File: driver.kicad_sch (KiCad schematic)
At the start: 83 parts, among them J2 Conn_02x07_Counter_Clockwise, Q1 RJK0355DSP, Q2 RJK0355DSP, Q3 SiRC18DP, Q4 SiRC18DP, Q5 SiRC18DP, Q6 SiRC18DP, U2 LM3743, U3 MAX1978, U4 INA333xxDGK

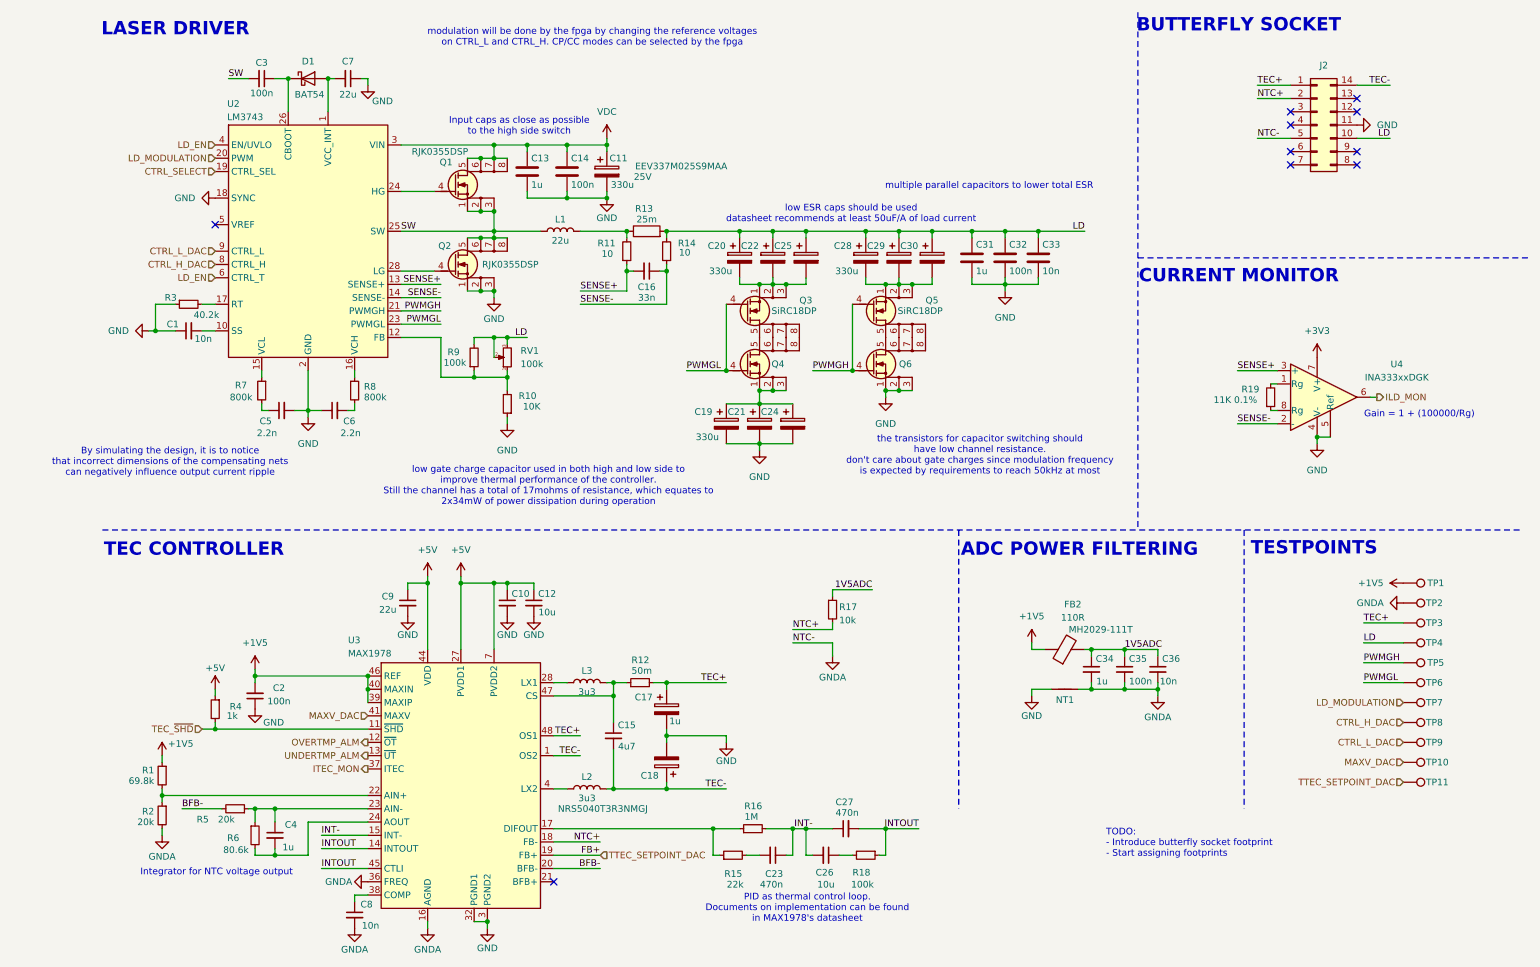
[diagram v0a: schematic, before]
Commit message: update PCB: fixed buck layout, concept layout for LD driver with LT3743
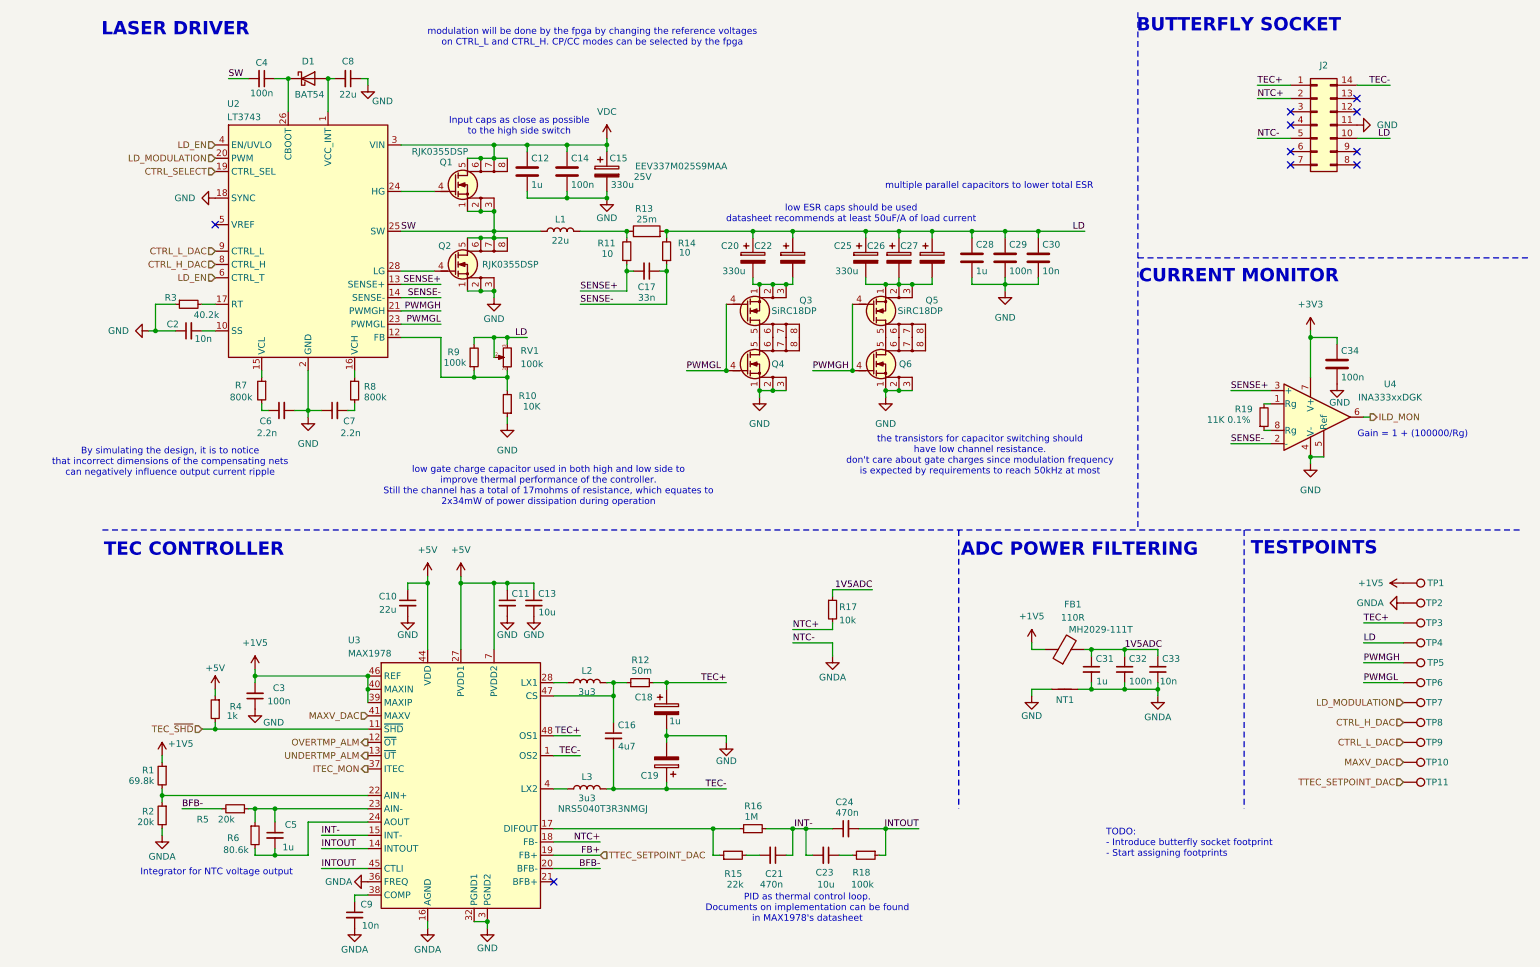
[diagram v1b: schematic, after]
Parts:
- removed C19, C21, C24, C25: 330u, Capacitor_SMD:CP_Elec_8x10.5, symbol Device:C_Polarized
- added C34: 100n, Capacitor_SMD:C_0805_2012Metric, symbol Device:C
- J2: footprint (none) -> footprints:Butterfly_14pins_SMD
- U2: value LM3743 -> LT3743
- renumbered C9 to C10, C10 to C11, C13 to C12, C12 to C13, C11 to C15, C15 to C16, C16 to C17, C17 to C18, C18 to C19, C1 to C2, C23 to C21, C26 to C23, C27 to C24, C28 to C25, C29 to C26, C30 to C27, C31 to C28, C32 to C29, C2 to C3, C33 to C30, C34 to C31, C35 to C32, C36 to C33, C3 to C4, C4 to C5, C5 to C6, C6 to C7, C7 to C8, C8 to C9, FB2 to FB1, L3 to L2, L2 to L3
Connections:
- net +3V3: now also C34.1
- net GND: now also Q4.1 (S), Q4.2 (S), Q4.3 (S), C34.2
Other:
- moved on the sheet: C20, C22, R19, U4

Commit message: Changed overall subsystem positions, TEC controller implemented, LD controller IC position to be reconsidered in order to have enough clearance after header connector is fully routed
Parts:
- added NT3: NetTie_2, NetTie:NetTie-2_SMD_Pad0.5mm, symbol Device:NetTie_2
- TP1, TP11: footprint TestPoint:TestPoint_Pad_D1.5mm -> TestPoint:TestPoint_Pad_D1.0mm
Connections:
- net AGND: now also NT3.2
- net GND: now also U3.49 (EP), NT3.1
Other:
- note removed: "TODO: - Introduce butterfly socket footprint - Start assigning footprints"

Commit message: PCB routing completed, started uniforming components for smaller BOM
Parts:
- C10, C11, C13, C21, C23, C24: footprint Capacitor_SMD:C_0805_2012Metric -> Capacitor_SMD:C_0603_1608Metric; Voltage Rating (none) -> 6V3
- C16, C8: Voltage Rating (none) -> 25V
- C17: Voltage Rating (none) -> 6V3
- C2, C30, C33, C9: Voltage Rating 25V -> 6V3
- C3, C31, C32, C34, C5: footprint Capacitor_SMD:C_0805_2012Metric -> Capacitor_SMD:C_0603_1608Metric; Voltage Rating 25V -> 6V3
- TP10: footprint TestPoint:TestPoint_Pad_D1.5mm -> TestPoint:TestPoint_Pad_D1.0mm

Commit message: small corrections to PCB, fixed some capacitors' voltage ratings and footprints to make BOM more uniform
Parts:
- C16: Voltage Rating 25V -> 16V
- C8: footprint Capacitor_SMD:C_0805_2012Metric -> Capacitor_SMD:C_0603_1608Metric; Voltage Rating 25V -> 6V3
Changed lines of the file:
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@@
 			)
 		)
-		(property "Footprint" "Capacitor_SMD:C_0805_2012Metric"
+		(property "Footprint" "Capacitor_SMD:C_0603_1608Metric"
 			(at 59.69 25.4 0)
 			(effects
@@
 			)
 		)
-		(property "Voltage Rating" "25V"
+		(property "Voltage Rating" "6V3"
 			(at 59.69 25.4 0)
 			(effects
@@
 			)
 		)
-		(property "Voltage Rating" "25V"
+		(property "Voltage Rating" "16V"
 			(at 110.49 151.13 0)
 			(effects

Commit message: feat: made possible to swap butterfly pins for compatibility
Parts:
- added J4: SELECTOR, Connector_PinHeader_2.54mm:PinHeader_2x09_P2.54mm_Vertical, symbol Connector_Generic:Conn_02x09_Odd_Even
- added J5: Conn_02x07_Counter_Clockwise, Connector_PinHeader_2.54mm:PinHeader_1x04_P2.54mm_Vertical, symbol Connector_Generic:Conn_01x04
- J2: value Conn_02x07_Counter_Clockwise -> BUTTERFLY
- TP2: footprint TestPoint:TestPoint_Pad_2.5x2.5mm -> TestPoint:TestPoint_Pad_1.5x1.5mm
- TP8, TP9: footprint TestPoint:TestPoint_Pad_D1.5mm -> TestPoint:TestPoint_Pad_D1.0mm
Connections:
- net AGND: now also J4.11 (Pin_11); no longer J2.5 (Pin_5)
- net GND: now also J4.3 (Pin_3), J4.5 (Pin_5); no longer J2.11 (Pin_11)
- net LD: now also J4.1 (Pin_1); no longer J2.10 (Pin_10)
- net NTC+: now also J4.13 (Pin_13); no longer J2.2 (Pin_2)
- net TEC+: now also J4.9 (Pin_9); no longer J2.1 (Pin_1)
- net TEC-: now also J4.7 (Pin_7); no longer J2.14 (Pin_14)
- net Pin_12: now reaches J2.12 (Pin_12)
- net Pin_12: now also J4.14 (Pin_14)
- net Pin_13: now reaches J2.13 (Pin_13)
- net Pin_13: now also J5.1 (Pin_1)
- net Pin_3: now reaches J2.3 (Pin_3)
- net Pin_3: now also J4.4 (Pin_4)
- net Pin_4: now reaches J2.4 (Pin_4)
- net Pin_4: now also J4.2 (Pin_2)
- net Pin_6: now reaches J2.6 (Pin_6)
- net Pin_6: now also J4.16 (Pin_16)
- net Pin_7: now reaches J2.7 (Pin_7)
- net Pin_7: now also J4.18 (Pin_18)
- net Pin_8: now reaches J2.8 (Pin_8)
- net Pin_8: now also J5.4 (Pin_4)
- net Pin_9: now reaches J2.9 (Pin_9)
- net Pin_9: now also J5.3 (Pin_3)
- new net Pin_1: J2.1 (Pin_1), J4.10 (Pin_10)
- new net Pin_10: J2.10 (Pin_10), J5.2 (Pin_2)
- new net Pin_11: J2.11 (Pin_11), J4.12 (Pin_12)
- new net Pin_14: J2.14 (Pin_14), J4.8 (Pin_8)
- new net Pin_2: J2.2 (Pin_2), J4.17 (Pin_17)
- new net Pin_5: J2.5 (Pin_5), J4.6 (Pin_6)
- no-connect marks 10 -> 3
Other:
- moved on the sheet: J2

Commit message: feat: added method to swap butterfly socket pins to adapt to multiple SOA SNs. Fixed routing imperfections and addes informative silkscreen
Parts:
- R12: value 50m -> 200m
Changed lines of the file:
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@@
 			)
 		)
-		(property "Value" "50m"
-			(at 117.856 138.684 90)
+		(property "Value" "200m"
+			(at 118.364 138.684 90)
 			(effects
 				(font

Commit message: fix: small corrections to the pcb, added PNs and store link to mouser for each component
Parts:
- C10, C8: PN (none) -> GRM188R60J226MEA0D; Store Link (none) -> https://www.mouser.it/ProductDetail/Murata-Electronics/GRM1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
- C11, C13, C23: PN (none) -> GRM188R60J106KE7J; Store Link (none) -> https://www.mouser.it/ProductDetail/Murata-Electronics/GRM1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
- C12, C28: PN (none) -> 885012207078; Store Link (none) -> https://www.mouser.it/ProductDetail/Wurth-Elektronik/885012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
- C14, C29, C4: PN (none) -> CL21F104ZBANNNC; Store Link (none) -> https://www.mouser.it/ProductDetail/Samsung-Electro-Mechani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
- C15, C20, C22, C25, C26, C27: Store Link (none) -> https://www.mouser.it/ProductDetail/KEMET/EEV337M025S9MAA?q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
- C16: PN (none) -> C1608X5R1E475K080AC; Store Link (none) -> https://www.mouser.it/ProductDetail/TDK/C1608X5R1E475K080AC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
- C17: PN (none) -> CGA3E2X7R1H333MA; Store Link (none) -> https://www.mouser.it/ProductDetail/KEMET/C0603C333M5RACTU?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
- C18, C19: PN EEV337M025S9MAA -> EDH105M050A9BAA; Store Link (none) -> https://www.mouser.it/ProductDetail/KEMET/EDH105M050A9BAA?q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
- C2, C30, C33, C9: PN (none) -> C0603C103M5RAC3121; Store Link (none) -> https://www.mouser.it/ProductDetail/KEMET/C0603C103M5RAC312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
- C21, C24: PN (none) -> 885012106020; Store Link (none) -> https://www.mouser.it/ProductDetail/Wurth-Elektronik/885012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
- C3, C32, C34: PN (none) -> CL10B104KB8NNND; Store Link (none) -> https://www.mouser.it/ProductDetail/Samsung-Electro-Mechani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
- C31, C5: PN (none) -> MCASE168SB7105KTNA01; Store Link (none) -> https://www.mouser.it/ProductDetail/TAIYO-YUDEN/MCASE168SB7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
- C6, C7: PN (none) -> C0603C222J3RACTU; Store Link (none) -> https://www.mouser.it/ProductDetail/KEMET/C0603C222J3RACTU?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
- D1: PN (none) -> BAT54; Store Link (none) -> https://www.mouser.it/ProductDetail/Diotec-Semiconductor/BA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; Voltage Rating (none) -> 30V
- FB1: Store Link (none) -> https://www.mouser.it/ProductDetail/Bourns/MH2029-111T?qs=H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
- J2, J4, TP1, TP10, TP11, TP2, TP3, TP4, TP5, TP6, TP7, TP8, TP9: now left out of the parts list
- J5: value Conn_02x07_Counter_Clockwise -> SELECTOR_2; now left out of the parts list
- L1: Store Link (none) -> https://www.mouser.it/ProductDetail/TAIYO-YUDEN/NRS8040T220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
- L2, L3: Store Link (none) -> https://www.mouser.it/ProductDetail/TAIYO-YUDEN/NRS5040T3R3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
- Q1, Q2: PN (none) -> RJK0355DSP; Store Link (none) -> https://www.mouser.it/ProductDetail/Renesas-Electronics/RJK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
- Q3, Q4, Q5, Q6: PN (none) -> SiRC18DP; Store Link (none) -> https://www.mouser.it/ProductDetail/Vishay-Semiconductors/S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
- R1: PN (none) -> ERJ-PB3B6982V; Store Link (none) -> https://www.mouser.it/ProductDetail/Panasonic/ERJ-PB3B6982V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
- R10: value 10K -> 1k; PN (none) -> RC0603FR-7W1KL; Store Link (none) -> https://www.mouser.it/ProductDetail/YAGEO/RC0603FR-7W1KL?qs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
- R11, R14: PN (none) -> CRCW060310R0FKEAC; Store Link (none) -> https://www.mouser.it/ProductDetail/Vishay-Dale/CRCW060310R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
- R12: PN (none) -> 560050350011; Store Link (none) -> https://www.mouser.it/ProductDetail/Wurth-Elektronik/560050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
- R13: value 25m -> 50m; PN (none) -> 560050332001; Store Link (none) -> https://www.mouser.it/ProductDetail/Wurth-Elektronik/560050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
- R15: PN (none) -> RC0603FR-7W22KL; Store Link (none) -> https://www.mouser.it/ProductDetail/YAGEO/RC0603FR-7W22KL?q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
- R16: PN (none) -> CRCW06031M00JNEA; Store Link (none) -> https://www.mouser.it/ProductDetail/Vishay-Dale/CRCW06031M0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
- R17: PN (none) -> CRCW060310K0FKEC; Store Link (none) -> https://www.mouser.it/ProductDetail/Vishay-Dale/CRCW060310K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
- R18: PN (none) -> RC0603FR-10100KL; Store Link (none) -> https://www.mouser.it/ProductDetail/YAGEO/RC0603FR-10100KL?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
- R19: PN (none) -> ERJ-PB3B1102V; Store Link (none) -> https://www.mouser.it/ProductDetail/Panasonic/ERJ-PB3B1102V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
- R2, R5: PN (none) -> ERJ-PB3B2002V; Store Link (none) -> https://www.mouser.it/ProductDetail/Panasonic/ERJ-PB3B2002V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
- R3: PN (none) -> ERJ-PB3B4022V; Store Link (none) -> https://www.mouser.it/ProductDetail/Panasonic/ERJ-PB3B4022V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
- R4: PN (none) -> RC0603FR-7W1KL; Store Link (none) -> https://www.mouser.it/ProductDetail/YAGEO/RC0603FR-7W1KL?qs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
- R6: PN (none) -> ERJ-3RBD8062V; Store Link (none) -> https://www.mouser.it/ProductDetail/Panasonic/ERJ-3RBD8062V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
- R7, R8: value 800k -> 806k; PN (none) -> CRCW0603806KFKEA; Store Link (none) -> https://www.mouser.it/ProductDetail/Vishay-Dale/CRCW0603806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
- R9: value 100k -> 2k2; PN (none) -> CRCW06032K20FKEA; Store Link (none) -> https://www.mouser.it/ProductDetail/Vishay-Dale/CRCW06032K2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
- RV1: value 100k -> 1k; footprint PCM_Potentiometer_SMD_AKL:Potentiometer_Bourns_3214W_Vertical -> PCM_Potentiometer_SMD_AKL:Potentiometer_Bourns_3224X_Vertical; PN (none) -> 3224X-2-102E; Store Link (none) -> https://www.mouser.it/ProductDetail/Bourns/3224X-2-102E?qs=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
- U2: PN (none) -> LT3743IFE#PBF; Store Link (none) -> https://www.mouser.it/ProductDetail/Analog-Devices/LT3743IF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
- U3: PN (none) -> MAX1979ETM+; Store Link (none) -> https://www.mouser.it/ProductDetail/Analog-Devices-Maxim-In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
- U4: PN (none) -> INA333AIDGKR; Store Link (none) -> https://www.mouser.it/ProductDetail/Texas-Instruments/INA33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
